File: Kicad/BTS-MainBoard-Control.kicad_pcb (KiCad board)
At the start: 2 copper layers, 26.8 x 45.1 mm, 24 parts, among them J3 Molex Micro Lock (1.25mm 1.5A), J4 Conn_01x14, U1 HIP4080A

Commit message: Moved Libraries folder and renamed project files
Signed-off-by: bebenlebricolo <benoittarrade@hotmail.fr>
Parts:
- J3: footprint PeltierSwitchingMainBoard_control:Molex_MicroLock_1.25_01x06 -> BTS-MainBoard-Control:Molex_MicroLock_1.25_01x06
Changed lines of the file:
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@@
     )
   )
-  (module PeltierSwitchingMainBoard_control:Molex_MicroLock_1.25_01x06 (layer F.Cu)
+  (module BTS-MainBoard-Control:Molex_MicroLock_1.25_01x06 (layer F.Cu)
     (at 78.105 41.91 180)
     (fp_text reference J3 (at -6.096 0.254 180) (layer F.SilkS)

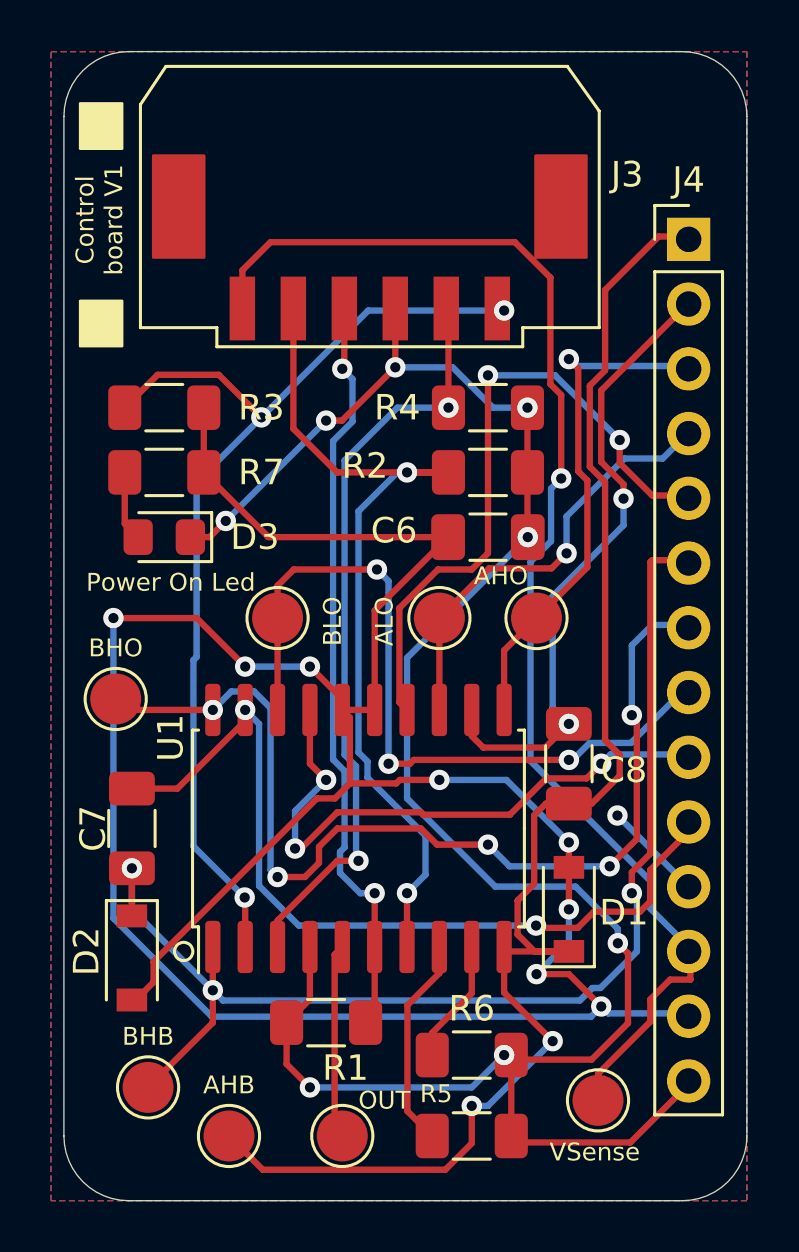
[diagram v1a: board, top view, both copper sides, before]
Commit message: Added power mosfet to drive cooling fans
Signed-off-by: bebenlebricolo <benoittarrade@hotmail.fr>
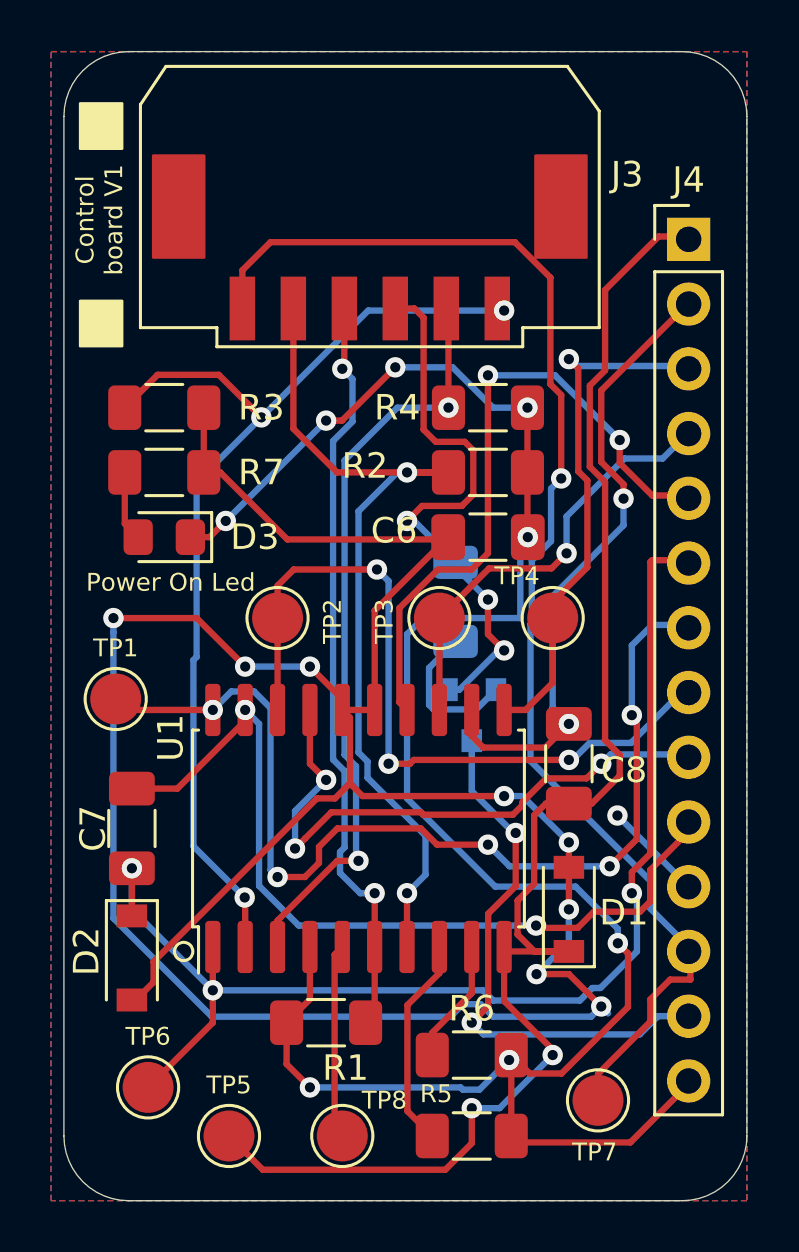
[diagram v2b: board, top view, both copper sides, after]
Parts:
- added Q1: DMG3402L, Package_TO_SOT_SMD:SOT-23, B.Cu at (78.1, 62.9)
- added R8: 56k, Resistor_SMD:R_1206_3216Metric_Pad1.30x1.75mm_HandSolder, B.Cu at (77.5, 58.4)
- moved TP4 0.64 mm to (81.3, 59.1)
- renumbered BHO to TP1, BLO to TP2, ALO to TP3, AHO to TP4, AHB to TP5, BHB to TP6, VSense to TP7, OUT to TP8
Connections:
- J3 pad 3: GND -> /Fan_trigger
- J4 pad 13: +12V -> /FanDrive
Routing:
- net /Fan_trigger: track 0.00 -> 22.4 mm, vias 0 -> 3
- net /FanDrive: track 0.00 -> 21.5 mm, vias 0 -> 2
- net GND: track 82.2 -> 88.4 mm
- net +12V: track 107.9 -> 105.0 mm
- net /AHO: track 20.3 -> 21.3 mm

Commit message: Replotted gerbers and updated silkscreen
Signed-off-by: bebenlebricolo <benoittarrade@hotmail.fr>
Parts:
- added REF**: OSHW-Logo2_14.6x12mm_SilkScreen, Symbol:OSHW-Logo2_14.6x12mm_SilkScreen, B.Cu at (76.2, 72.4)

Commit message: Refill zones
Signed-off-by: bebenlebricolo <benoittarrade@hotmail.fr>
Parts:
- removed REF**: OSHW-Logo2_14.6x12mm_SilkScreen, Symbol:OSHW-Logo2_14.6x12mm_SilkScreen
